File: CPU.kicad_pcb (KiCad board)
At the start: 4 copper layers, 364 x 203 mm, 219 parts, among them J1 Conn_02x36_Top_Bottom, P10 Conn_02x08_Counter_Clockwise, P2 Conn_02x13_Top_Bottom, P3 Conn_02x13_Top_Bottom, P4 Conn_02x08_Counter_Clockwise, P5 Conn_02x25_Counter_Clockwise, P6 Conn_02x25_Counter_Clockwise, P7 Conn_02x07_Counter_Clockwise, P8 Conn_02x08_Counter_Clockwise

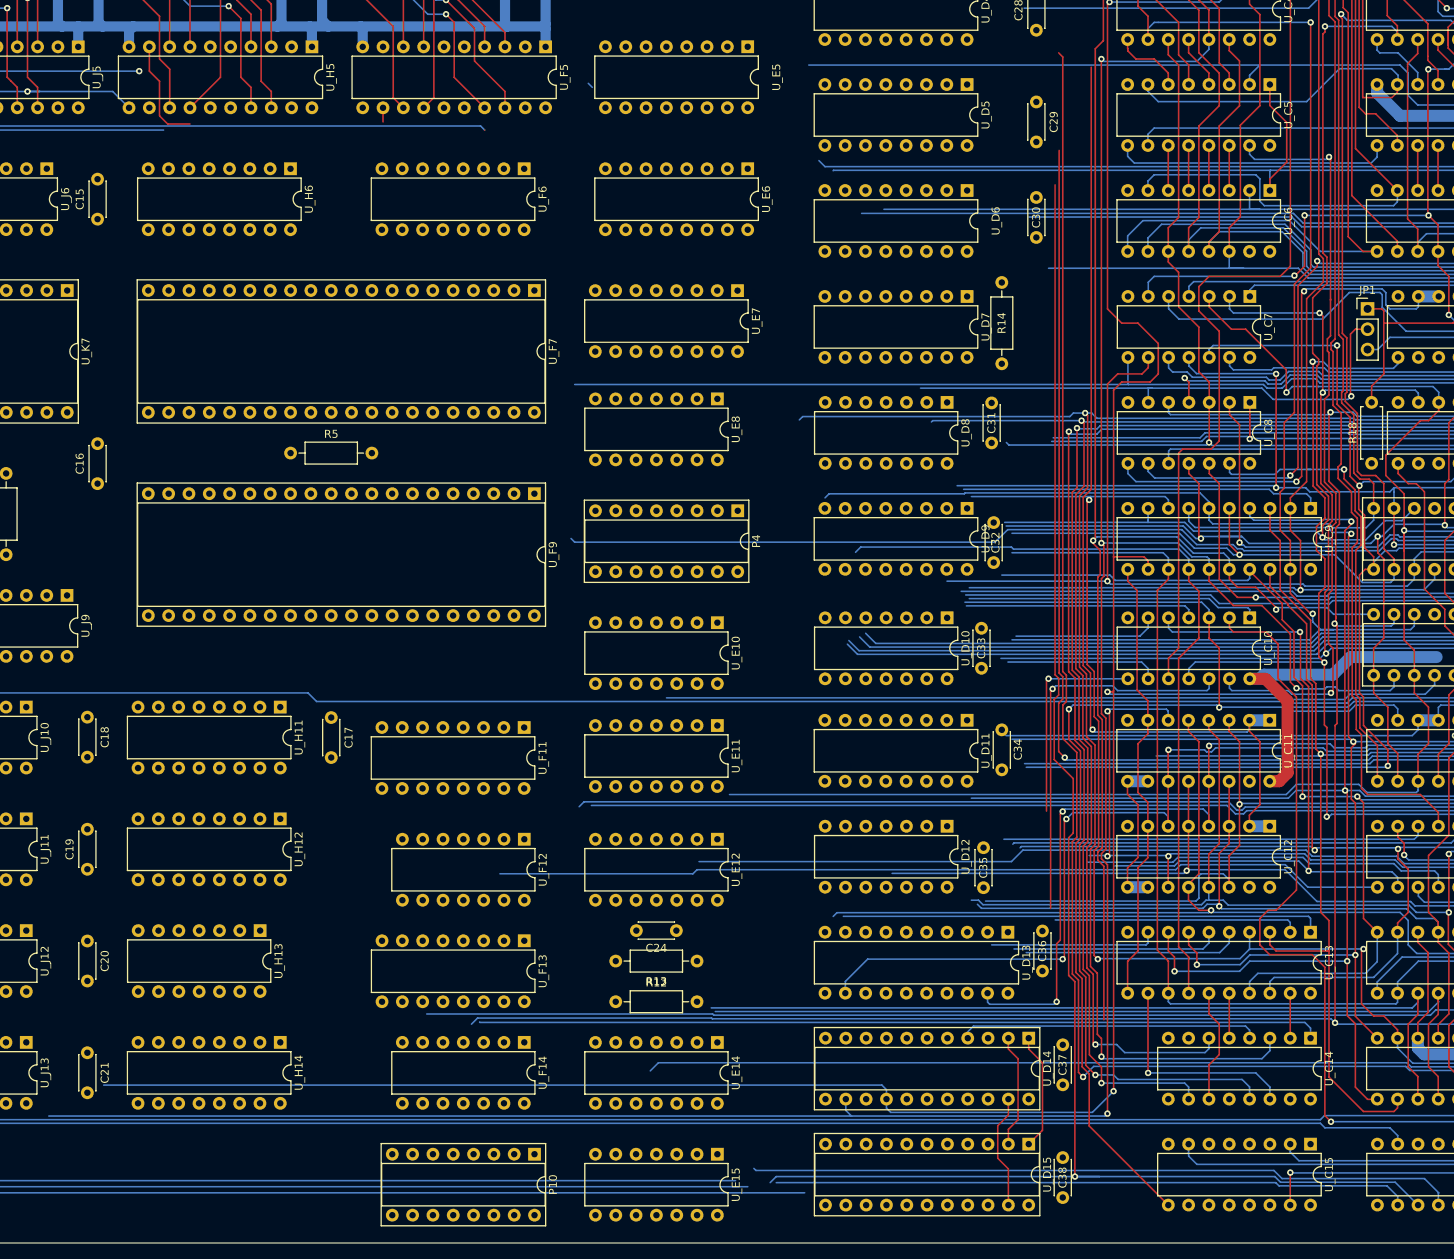
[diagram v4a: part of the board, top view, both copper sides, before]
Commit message: 4rth row placement
PoC placement, optimized tracks layout, Result bus moved to the right side. A
checkpoint before moving the whole row.
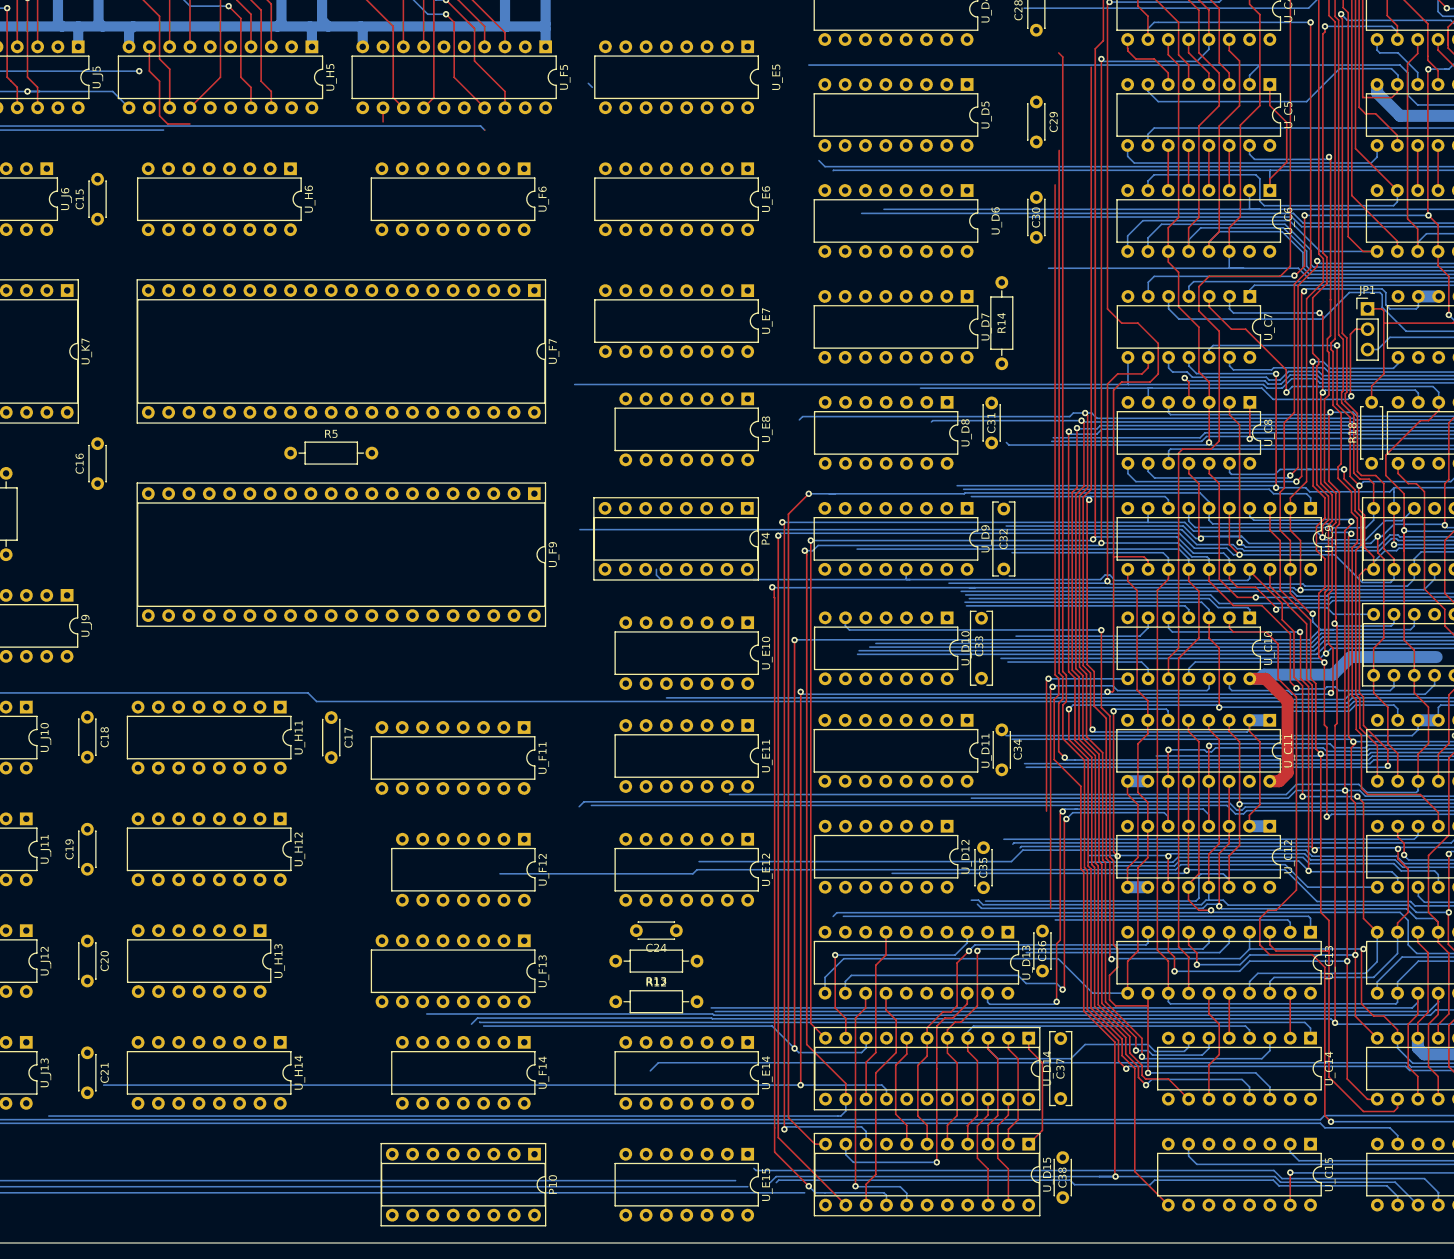
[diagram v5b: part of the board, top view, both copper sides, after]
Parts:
- C32, C33, C37: footprint Capacitor_THT:C_Disc_D4.3mm_W1.9mm_P5.00mm -> Capacitor_THT:C_Rect_L9.0mm_W2.5mm_P7.50mm_MKT
- moved U_E10 3.79 mm to (236.2, 149.5)
- moved U_E11 3.79 mm to (236.2, 162.3)
- moved U_E12 3.79 mm to (236.2, 176.5)
- moved U_E14 3.79 mm to (236.2, 201.9)
- moved U_E15 3.79 mm to (236.2, 215.9)
- moved U_E8 3.79 mm to (236.2, 121.5)
- moved C37 1.74 mm to (275.3, 208.9)
- moved C32 1.50 mm to (268.2, 142.7)
- moved U_E7 1.27 mm to (236.2, 108.0)
- moved C33 1.25 mm to (265.4, 156.4)
- moved P4 1.23 mm to (236.2, 135.2)
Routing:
- net Res.D_{7}: track 178.8 -> 307.7 mm, vias 2 -> 4
- net Res.D_{1}: track 162.5 -> 279.1 mm, vias 2 -> 3
- net Res.D_{3}: track 155.0 -> 270.9 mm, vias 2 -> 4
- net Res.D_{0}: track 176.2 -> 289.7 mm, vias 2 -> 4
- net Res.D_{2}: track 159.7 -> 247.3 mm, vias 1 -> 2
- net Net-(U_C13-Pad12): track 27.4 -> 113.3 mm, vias 1 -> 2
- net DataF.D_{6}: track 155.9 -> 202.5 mm
- net Net-(U_C14-Pad7): track 0.00 -> 43.7 mm
- net /~{ClockB_{2}}: track 56.1 -> 98.6 mm
- net Res.D_{6}: track 187.4 -> 224.4 mm, vias 3 -> 4
- net Net-(U_D13-Pad18): track 0.00 -> 36.4 mm, vias 0 -> 1
- net Net-(U_D13-Pad13): track 0.00 -> 32.9 mm, vias 0 -> 1
- net Net-(U_C13-Pad6): track 26.0 -> 57.9 mm, vias 0 -> 1
- net Net-(U_C13-Pad9): track 21.0 -> 52.0 mm, vias 0 -> 1
- net Net-(U_D13-Pad3): track 0.00 -> 29.4 mm, vias 0 -> 1
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
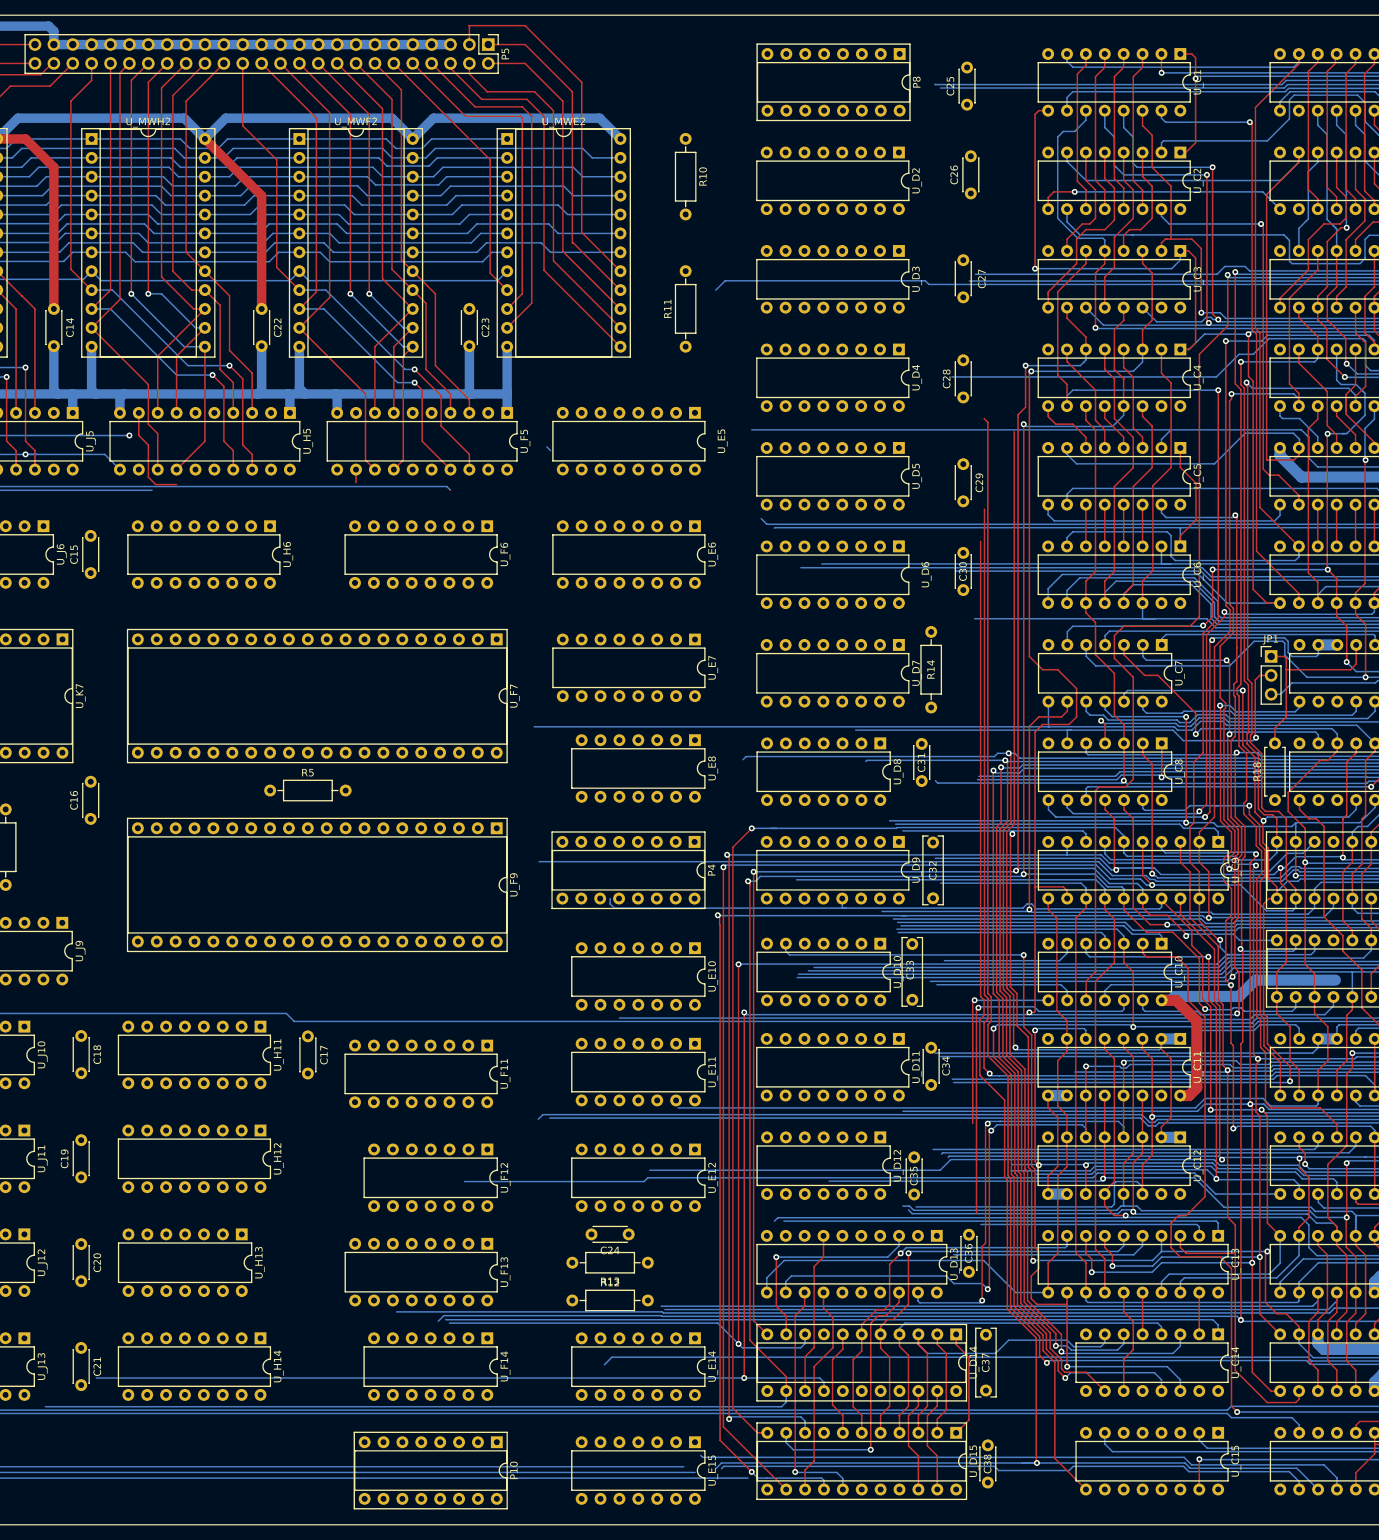
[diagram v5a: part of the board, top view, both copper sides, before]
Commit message: Move completed
Now we have much more space between 4th and 5th rows for tracks
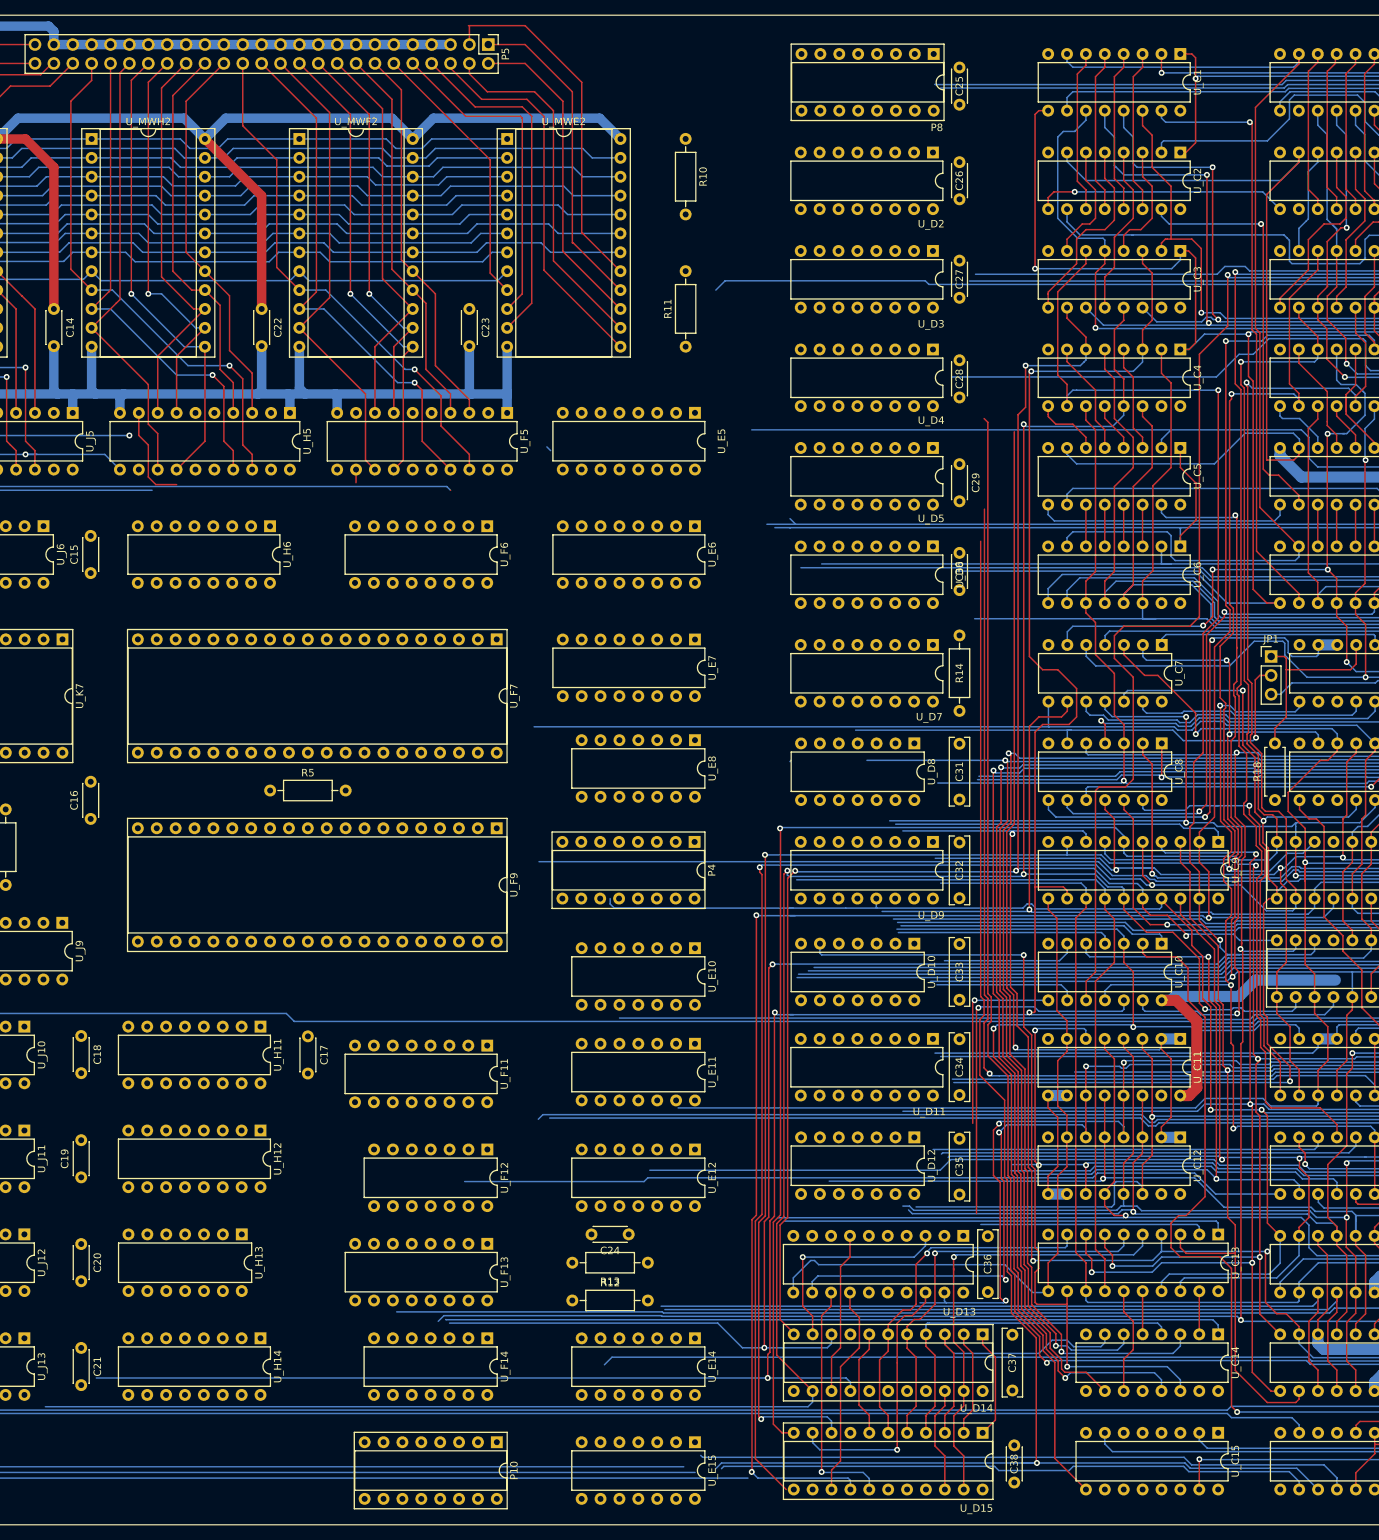
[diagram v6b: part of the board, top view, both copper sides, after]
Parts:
- C31, C34, C35, C36: footprint Capacitor_THT:C_Disc_D4.3mm_W1.9mm_P5.00mm -> Capacitor_THT:C_Rect_L9.0mm_W2.5mm_P7.50mm_MKT
- moved C33 6.35 mm to (271.8, 156.4)
- moved C35 6.10 mm to (271.8, 182.6)
- moved C31 5.66 mm to (271.8, 129.5)
- moved C27 5.09 mm to (271.8, 62.0), turned to 90 degrees
- moved P8 4.58 mm to (268.3, 29.2)
- moved U_D10 4.58 mm to (265.7, 148.9)
- moved U_D11 4.58 mm to (268.2, 161.7)
- moved U_D12 4.58 mm to (265.7, 174.9)
- moved U_D2 4.58 mm to (268.2, 42.5)
- moved U_D3 4.58 mm to (268.2, 55.7)
- moved U_D4 4.58 mm to (268.2, 68.9)
- moved U_D5 4.58 mm to (268.2, 82.2)
- moved U_D6 4.58 mm to (268.2, 95.4)
- moved U_D7 4.58 mm to (268.2, 108.7)
- moved U_D8 4.58 mm to (265.7, 121.9)
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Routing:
- net /CPL_{3}: track 227.7 -> 191.6 mm
- net Net-(U_C13-Pad5): track 41.6 -> 61.0 mm, vias 0 -> 1
- net Res.D_{1}: track 279.1 -> 272.9 mm
- net Res.D_{2}: track 247.3 -> 241.4 mm
- net Res.D_{3}: track 270.9 -> 265.5 mm
- net Net-(U_C13-Pad12): track 113.3 -> 108.4 mm
- net Res.D_{6}: track 224.4 -> 219.8 mm
- net DataP.D_{0}: track 309.3 -> 305.4 mm
- net Net-(U_C13-Pad9): track 52.0 -> 48.3 mm
- net Net-(U_C14-Pad7): track 43.7 -> 40.1 mm
- net /~{ClockB_{2}}: track 98.6 -> 95.1 mm
- net Net-(U_C13-Pad6): track 57.9 -> 54.3 mm
- net Res.D_{0}: track 289.7 -> 286.5 mm
- net Net-(U_C14-Pad4): track 51.8 -> 48.6 mm
- net DataP.D_{3}: track 305.4 -> 308.0 mm
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
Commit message: Some more connections
WIP
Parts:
- moved C29 3.48 mm to (271.8, 87.8), turned to 90 degrees
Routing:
- net /~{Reg_OE}: track 0.00 -> 133.2 mm
- net DataP.D_{4}: track 310.0 -> 440.8 mm, vias 5 -> 6
- net Net-(U_C10-Pad4): track 29.0 -> 141.1 mm, vias 0 -> 1
- net /MainClockPhi1: track 36.7 -> 146.0 mm
- net /BeginWrite: track 19.1 -> 116.3 mm
- net DataP.D_{5}: track 286.8 -> 378.5 mm
- net /MWR.H0_{0}: track 36.8 -> 113.6 mm
- net /MWR.H0_{1}: track 44.3 -> 119.6 mm
- net /PTR.~{Q_{7}}: track 67.2 -> 140.5 mm, vias 1 -> 2
- net /MemFault_EN: track 66.6 -> 139.8 mm
- net /~{ClockB_{2}}: track 95.1 -> 167.4 mm
- net /MWR.H0_{3}: track 51.1 -> 118.3 mm
- net Net-(U_A1-Pad4): track 90.7 -> 157.4 mm
- net /DMA.Write: track 0.00 -> 66.3 mm, vias 0 -> 1
- net Net-(U_B11-Pad6): track 155.1 -> 220.3 mm, vias 2 -> 3
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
